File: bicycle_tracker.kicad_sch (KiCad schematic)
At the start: 17 parts, among them J1 USB_C_KH-TYPE-C-16P, U1 SAM-M8Q, U2 24LC64, U3 ICM-20948, U4 W25Q32JVZP, U5 ESP32-C6, U6 BQ24040, U7 SX1262

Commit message: Checkpoint
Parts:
- removed U7: SX1262, Package_DFN_QFN:QFN-24-1EP_4x4mm_P0.5mm_EP2.7x2.7mm, symbol bicycle_tracker:SX1262
- added C1: 100nF, symbol Device:C_Small
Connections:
- net GND: now also C1.1
- net VDD_SPI: now also C1.2
- net UART_MRXSTX: no longer names the net of U5.10 (GPIO4)
- net UART_MRXSTX: no longer U1.13 (TXD)
- net UART_MTXSRX: no longer names the net of U5.11 (GPIO5)
- net UART_MTXSRX: no longer U1.14 (RXD)
- no-connect marks 4 -> 6
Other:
- added sheet LoRa Radio (lora_radio.kicad_sch)

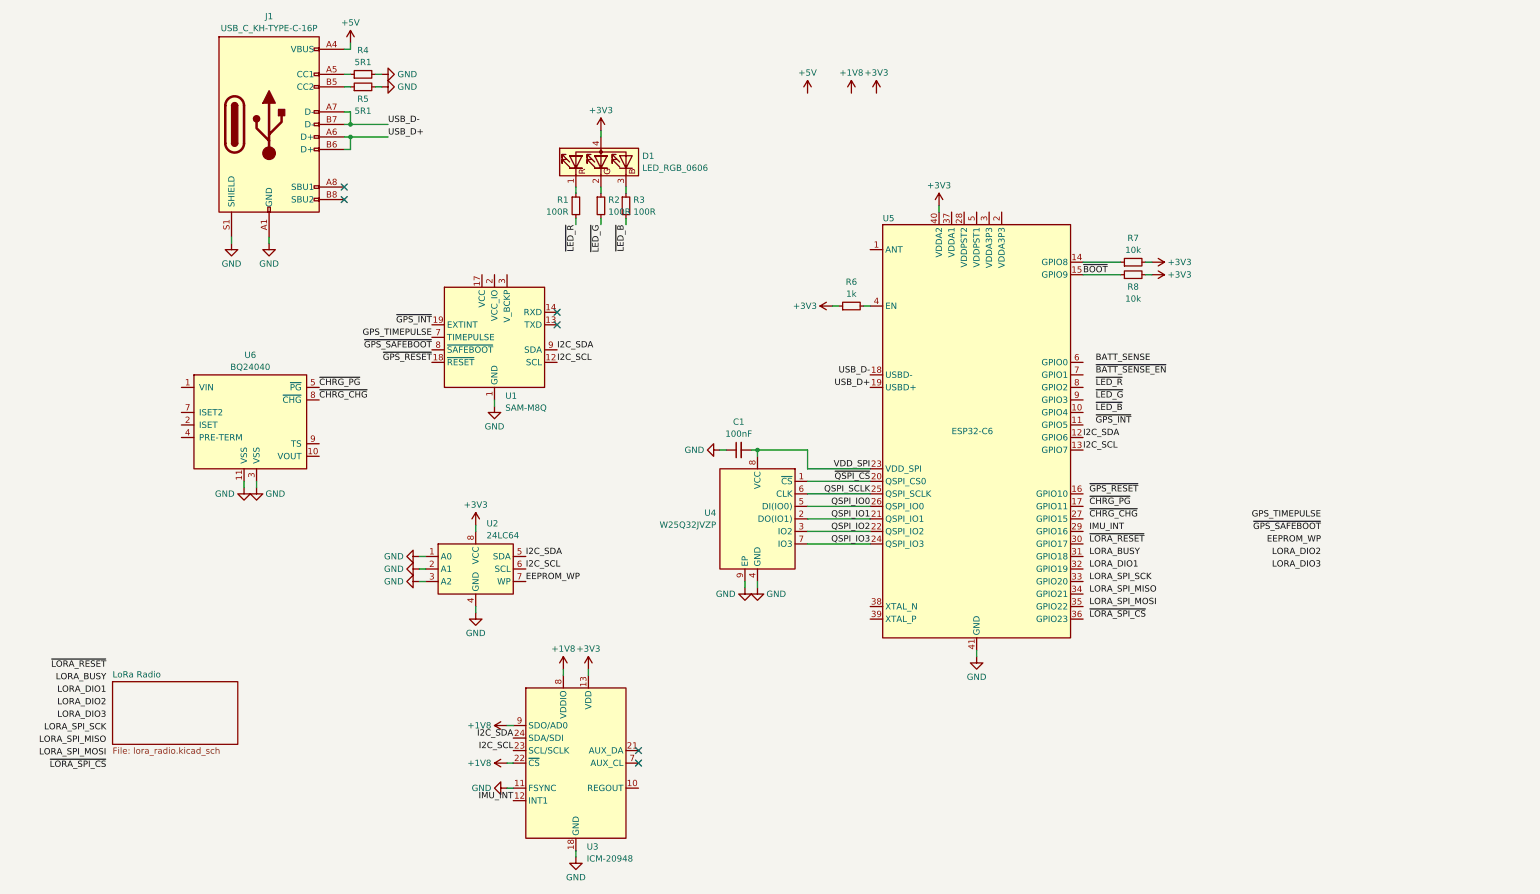
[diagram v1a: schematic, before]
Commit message: Swapped to NRF and made a bunch of progress
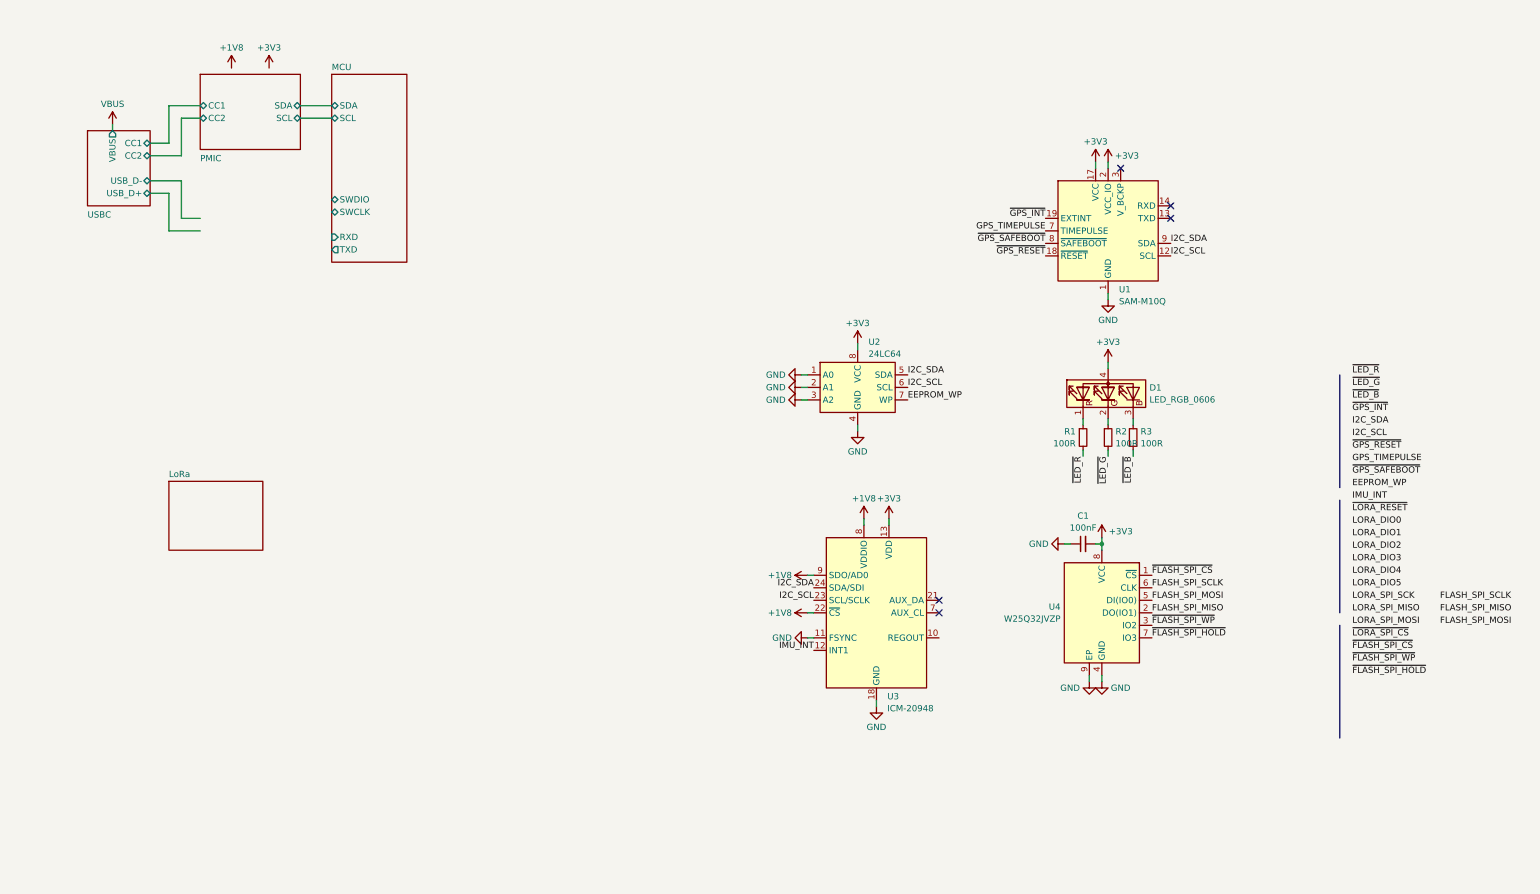
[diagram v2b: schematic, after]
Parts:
- removed J1: USB_C_KH-TYPE-C-16P, plentify_footprints:USB_C_Receptacle_KH-TYPE-C-16P, symbol plentify_symbols:USB_C_KH-TYPE-C-16P
- removed R4, R5: 5R1, symbol Device:R_Small
- removed R6: 1k, symbol Device:R_Small
- removed R7, R8: 10k, symbol Device:R_Small
- removed U5: ESP32-C6, bicycle_tracker:QFN-40-1EP_5x5mm_P0.4mm_EP3.3x3.3mm, symbol bicycle_tracker:ESP32-C6
- removed U6: BQ24040, bicycle_tracker:PWSON-N10-2x2, symbol bicycle_tracker:BQ24040
- C1: footprint (none) -> Capacitor_SMD:C_0402_1005Metric
- R1, R2, R3: footprint (none) -> Resistor_SMD:R_0402_1005Metric
- U1: value SAM-M8Q -> SAM-M10Q
- U2: footprint (none) -> Package_SO:TSSOP-8_4.4x3mm_P0.65mm
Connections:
- net VDD_SPI is gone; now on net +3V3: C1.2, U4.8 (VCC)
- net +3V3: now also U1.17 (VCC), U1.2 (VCC_IO)
- net QSPI_IO0 renamed FLASH_SPI_MOSI
- net QSPI_IO1 renamed FLASH_SPI_MISO
- net QSPI_IO2 renamed ~{FLASH_SPI_WP}
- net QSPI_IO3 renamed ~{FLASH_SPI_HOLD}
- net QSPI_SCLK renamed FLASH_SPI_SCLK
- net ~{QSPI_CS} renamed ~{FLASH_SPI_CS}
- no-connect marks 6 -> 5
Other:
- removed sheet LoRa Radio
- added sheet LoRa (lora.kicad_sch)
- added sheet MCU (mcu.kicad_sch)
- added sheet PMIC (pmic.kicad_sch)
- added sheet USBC (usbc.kicad_sch)
- moved on the sheet: C1, D1, R1, R2, R3, U1, U2, U3, U4
